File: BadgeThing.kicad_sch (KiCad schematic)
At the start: 62 parts, among them J2 Ext 5V, J3 External 3V3, J4 SWD Header, J5 USB_C_Receptacle_USB2.0, J6 Connector_Generic_Conn_01x02, J7 Conn_01x06, SW1 ESP RESET, SW2 Left, SW3 Down, SW4 Select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

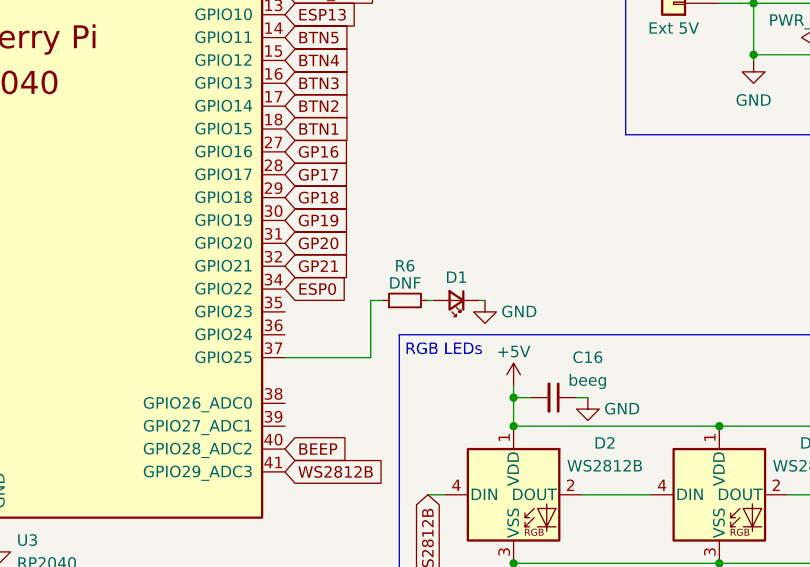
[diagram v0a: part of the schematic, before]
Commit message: Update 3D models
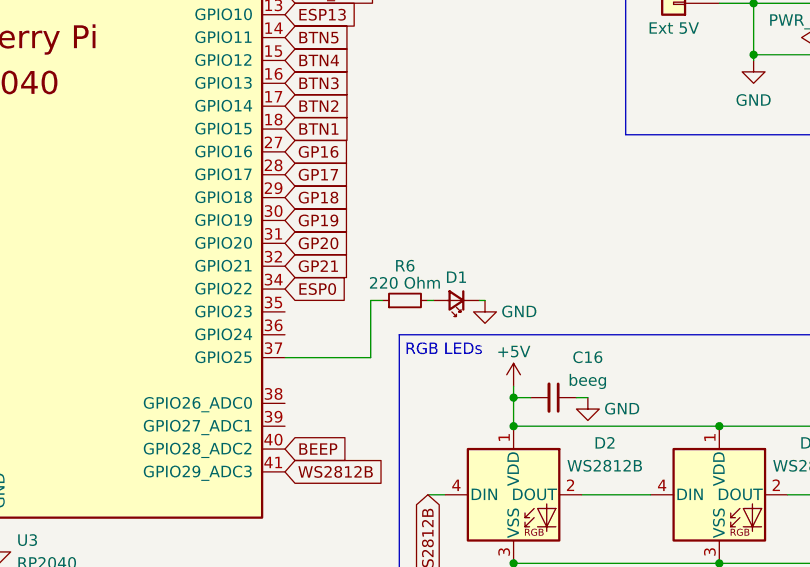
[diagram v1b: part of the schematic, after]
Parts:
- R6: value DNF -> 220 Ohm
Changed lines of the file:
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@@
       (effects (font (size 1.27 1.27)))
     )
-    (property "Value" "DNF" (at 167.005 113.665 90)
+    (property "Value" "220 Ohm" (at 167.005 113.665 90)
       (effects (font (size 1.27 1.27)))
     )

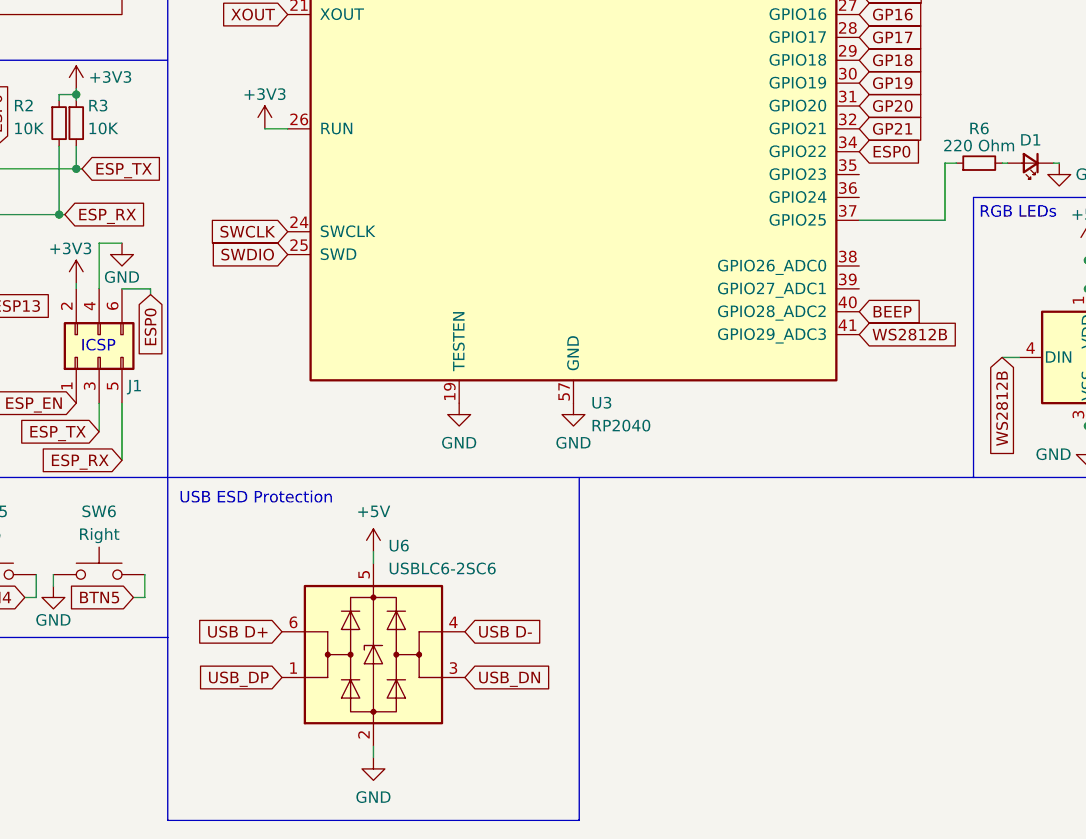
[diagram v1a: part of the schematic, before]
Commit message: consider adding an SD card slot
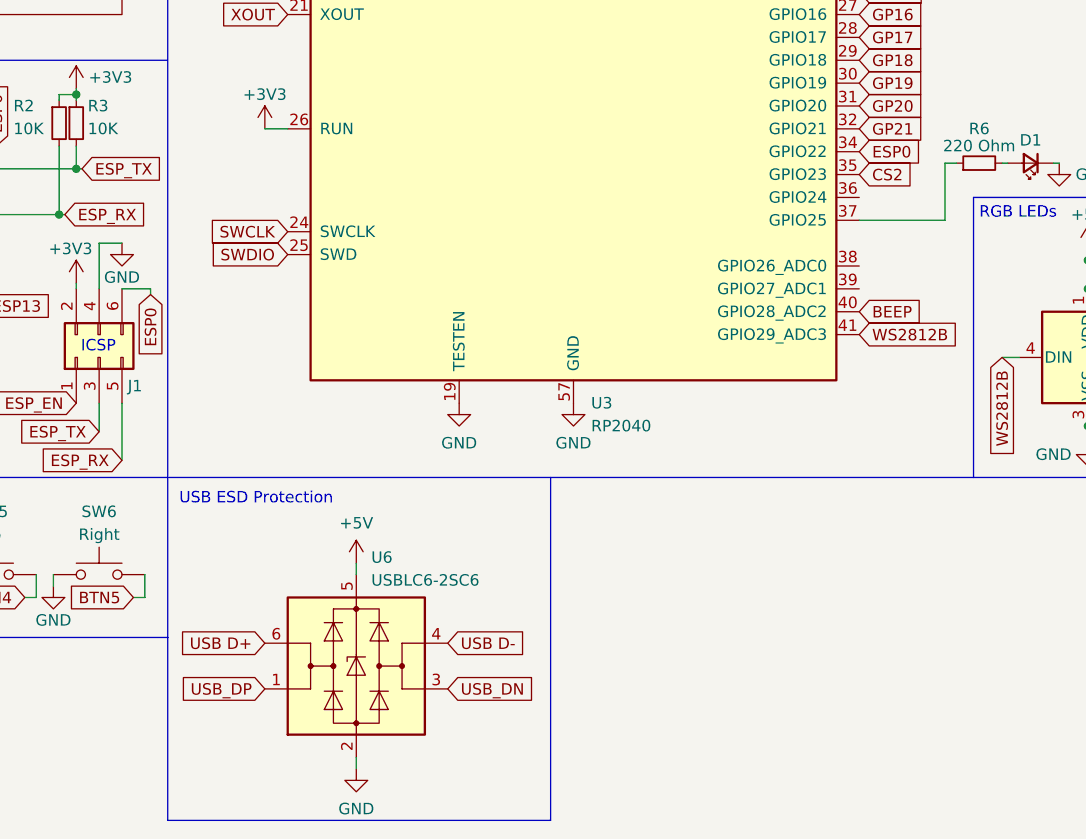
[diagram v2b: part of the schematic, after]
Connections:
- net CS2: now reaches U3.35 (GPIO23)
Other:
- moved on the sheet: U6
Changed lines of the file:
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@@
     (stroke (width 0) (type default))
   )
-  (polyline (pts (xy 76.835 188.595) (xy 122.555 188.595))
+  (polyline (pts (xy 76.835 188.595) (xy 119.38 188.595))
     (stroke (width 0) (type default))
   )
-  (wire (pts (xy 99.695 180.34) (xy 99.695 181.61))
+  (wire (pts (xy 97.79 181.61) (xy 97.79 182.88))
     (stroke (width 0) (type default))
   )
@@
     (stroke (width 0) (type default))
   )
-  (polyline (pts (xy 122.555 188.595) (xy 122.555 150.495))
+  (polyline (pts (xy 119.38 188.595) (xy 119.38 150.495))
     (stroke (width 0) (type default))
   )
@@
     (stroke (width 0) (type default))
   )
-  (wire (pts (xy 99.695 158.75) (xy 99.695 160.02))
+  (wire (pts (xy 97.79 160.02) (xy 97.79 161.29))
     (stroke (width 0) (type default))
   )
@@
     )
   )
-  (global_label "USB D-" (shape input) (at 109.855 167.64 0) (fields_autoplaced)
+  (global_label "USB D-" (shape input) (at 107.95 168.91 0) (fields_autoplaced)
     (effects (font (size 1.27 1.27)) (justify left))
-    (property "Intersheetrefs" "${INTERSHEET_REFS}" (at 120.3808 167.64 0)
+    (property "Intersheetrefs" "${INTERSHEET_REFS}" (at 118.4758 168.91 0)
       (effects (font (size 1.27 1.27)) (justify left) hide)
     )
@@
     )
   )
-  (global_label "USB_DP" (shape input) (at 89.535 172.72 180) (fields_autoplaced)
+  (global_label "USB_DP" (shape input) (at 87.63 173.99 180) (fields_autoplaced)
     (effects (font (size 1.27 1.27)) (justify right))
-    (property "Intersheetrefs" "${INTERSHEET_REFS}" (at 79.3116 172.72 0)
+    (property "Intersheetrefs" "${INTERSHEET_REFS}" (at 77.4066 173.99 0)
       (effects (font (size 1.27 1.27)) (justify right) hide)
     )
@@
     )
   )
+  (global_label "CS2" (shape input) (at 153.67 116.84 0) (fields_autoplaced)
+    (effects (font (size 1.27 1.27)) (justify left))
+    (property "Intersheetrefs" "${INTERSHEET_REFS}" (at 160.2648 116.84 0)
+      (effects (font (size 1.27 1.27)) (justify left) hide)
+    )
+  )
   (global_label "BEEP" (shape input) (at 273.685 125.095 180) (fields_autoplaced)
     (effects (font (size 1.27 1.27)) (justify right))
@@
     )
   )
-  (global_label "USB_DN" (shape input) (at 109.855 172.72 0) (fields_autoplaced)
+  (global_label "USB_DN" (shape input) (at 107.95 173.99 0) (fields_autoplaced)
     (effects (font (size 1.27 1.27)) (justify left))
-    (property "Intersheetrefs" "${INTERSHEET_REFS}" (at 120.1389 172.72 0)
+    (property "Intersheetrefs" "${INTERSHEET_REFS}" (at 118.2339 173.99 0)
       (effects (font (size 1.27 1.27)) (justify left) hide)
     )
@@
     )
   )
-  (global_label "USB D+" (shape input) (at 89.535 167.64 180) (fields_autoplaced)
+  (global_label "USB D+" (shape input) (at 87.63 168.91 180) (fields_autoplaced)
     (effects (font (size 1.27 1.27)) (justify right))
-    (property "Intersheetrefs" "${INTERSHEET_REFS}" (at 79.0092 167.64 0)
+    (property "Intersheetrefs" "${INTERSHEET_REFS}" (at 77.1042 168.91 0)
       (effects (font (size 1.27 1.27)) (justify right) hide)
     )
@@
     )
   )
-  (symbol (lib_name "+5V_2") (lib_id "power:+5V") (at 99.695 158.75 0) (unit 1)
+  (symbol (lib_name "+5V_2") (lib_id "power:+5V") (at 97.79 160.02 0) (unit 1)
     (in_bom yes) (on_board yes) (dnp no) (fields_autoplaced)
-    (property "Reference" "#PWR044" (at 99.695 162.56 0)
+    (property "Reference" "#PWR044" (at 97.79 163.83 0)
       (effects (font (size 1.27 1.27)) hide)
     )
-    (property "Value" "+5V" (at 99.695 154.305 0)
+    (property "Value" "+5V" (at 97.79 155.575 0)
       (effects (font (size 1.27 1.27)))
     )
-    (property "Footprint" "" (at 99.695 158.75 0)
+    (property "Footprint" "" (at 97.79 160.02 0)
       (effects (font (size 1.27 1.27)) hide)
     )
-    (property "Datasheet" "" (at 99.695 158.75 0)
+    (property "Datasheet" "" (at 97.79 160.02 0)
       (effects (font (size 1.27 1.27)) hide)
     )
@@
     )
   )
-  (symbol (lib_id "Power_Protection:USBLC6-2SC6") (at 99.695 170.18 0) (unit 1)
+  (symbol (lib_id "Power_Protection:USBLC6-2SC6") (at 97.79 171.45 0) (unit 1)
     (in_bom yes) (on_board yes) (dnp no) (fields_autoplaced)
-    (property "Reference" "U6" (at 101.3461 158.115 0)
+    (property "Reference" "U6" (at 99.4411 159.385 0)
       (effects (font (size 1.27 1.27)) (justify left))
     )
-    (property "Value" "USBLC6-2SC6" (at 101.3461 160.655 0)
+    (property "Value" "USBLC6-2SC6" (at 99.4411 161.925 0)
       (effects (font (size 1.27 1.27)) (justify left))
     )
-    (property "Footprint" "Package_TO_SOT_SMD:SOT-23-6" (at 99.695 182.88 0)
+    (property "Footprint" "Package_TO_SOT_SMD:SOT-23-6" (at 97.79 184.15 0)
       (effects (font (size 1.27 1.27)) hide)
     )
-    (property "Datasheet" "https://www.st.com/resource/en/datasheet/usblc6-2.pdf" (at 104.775 161.29 0)
+    (property "Datasheet" "https://www.st.com/resource/en/datasheet/usblc6-2.pdf" (at 102.87 162.56 0)
       (effects (font (size 1.27 1.27)) hide)
     )
-    (property "LCSC" "C2687116" (at 99.695 170.18 0)
+    (property "LCSC" "C2687116" (at 97.79 171.45 0)
       (effects (font (size 1.27 1.27)) hide)
     )
@@
     )
   )
-  (symbol (lib_id "power:GND") (at 99.695 181.61 0) (unit 1)
+  (symbol (lib_id "power:GND") (at 97.79 182.88 0) (unit 1)
     (in_bom yes) (on_board yes) (dnp no) (fields_autoplaced)
-    (property "Reference" "#PWR045" (at 99.695 187.96 0)
+    (property "Reference" "#PWR045" (at 97.79 189.23 0)
       (effects (font (size 1.27 1.27)) hide)
     )
-    (property "Value" "GND" (at 99.695 186.055 0)
+    (property "Value" "GND" (at 97.79 187.325 0)
       (effects (font (size 1.27 1.27)))
     )
-    (property "Footprint" "" (at 99.695 181.61 0)
+    (property "Footprint" "" (at 97.79 182.88 0)
       (effects (font (size 1.27 1.27)) hide)
     )
-    (property "Datasheet" "" (at 99.695 181.61 0)
+    (property "Datasheet" "" (at 97.79 182.88 0)
       (effects (font (size 1.27 1.27)) hide)
     )

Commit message: Actual final real finishing touches (+test pads)
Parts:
- added J10, J11, J12, J8, J9: Conn_01x01, Connector_PinHeader_2.00mm:PinHeader_1x01_P2.00mm_Vertical, symbol Connector_Generic:Conn_01x01
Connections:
- net +3V3: now also J12.1 (Pin_1)
- net +5V: now also J11.1 (Pin_1)
- net MISO: now also J8.1 (Pin_1)
- net MOSI: now also J9.1 (Pin_1)
- net SCLK: now also J10.1 (Pin_1)
- net CS2: no longer names the net of U3.35 (GPIO23)
- no-connect marks 24 -> 29
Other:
- note added: "Test Points"
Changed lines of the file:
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@@
   (no_connect (at 269.875 100.33))
   (no_connect (at 55.88 139.065))
+  (no_connect (at 153.67 127))
   (no_connect (at 45.085 83.82))
   (no_connect (at 55.88 133.985))
@@
   (no_connect (at 55.88 128.905))
   (no_connect (at 45.085 76.2))
+  (no_connect (at 153.67 66.04))
+  (no_connect (at 153.67 129.54))
+  (no_connect (at 153.67 119.38))
+  (no_connect (at 153.67 116.84))
   (wire (pts (xy 45.085 45.72) (xy 43.815 45.72))
     (stroke (width 0) (type default))
@@
     (stroke (width 0) (type default))
   )
+  (wire (pts (xy 132.08 170.18) (xy 128.905 170.18))
+    (stroke (width 0) (type default))
+  )
   (wire (pts (xy 194.31 43.18) (xy 198.12 43.18))
     (stroke (width 0) (type default))
@@
     (stroke (width 0) (type default))
   )
+  (wire (pts (xy 122.555 166.37) (xy 132.08 166.37))
+    (stroke (width 0) (type default))
+  )
   (wire (pts (xy 155.575 38.1) (xy 155.575 31.75))
     (stroke (width 0) (type default))
@@
     (stroke (width 0) (type default))
   )
+  (wire (pts (xy 132.08 168.91) (xy 132.08 170.18))
+    (stroke (width 0) (type default))
+  )
   (wire (pts (xy 43.815 60.96) (xy 43.815 63.5))
     (stroke (width 0) (type default))
@@
     (effects (font (size 1.27 1.27)) (justify left bottom))
   )
+  (text "Test Points" (at 120.65 153.67 0)
+    (effects (font (size 1.27 1.27)) (justify left bottom))
+  )
   (text "Voltage Regulator" (at 193.802 64.2874 0)
     (effects (font (size 1.27 1.27)) (justify left bottom))
@@
     )
   )
+  (global_label "SCLK" (shape input) (at 132.08 163.83 180) (fields_autoplaced)
+    (effects (font (size 1.27 1.27)) (justify right))
+    (property "Intersheetrefs" "${INTERSHEET_REFS}" (at 124.3966 163.83 0)
+      (effects (font (size 1.27 1.27)) (justify right) hide)
+    )
+  )
   (global_label "SCLK" (shape input) (at 26.035 66.04 180) (fields_autoplaced)
     (effects (font (size 1.27 1.27)) (justify right))
@@
     )
   )
+  (global_label "MOSI" (shape input) (at 132.08 161.29 180) (fields_autoplaced)
+    (effects (font (size 1.27 1.27)) (justify right))
+    (property "Intersheetrefs" "${INTERSHEET_REFS}" (at 124.578 161.29 0)
+      (effects (font (size 1.27 1.27)) (justify right) hide)
+    )
+  )
   (global_label "ESP_TX" (shape input) (at 69.215 145.415 180) (fields_autoplaced)
     (effects (font (size 1.27 1.27)) (justify right))
@@
     )
   )
-  (global_label "CS2" (shape input) (at 153.67 116.84 0) (fields_autoplaced)
-    (effects (font (size 1.27 1.27)) (justify left))
-    (property "Intersheetrefs" "${INTERSHEET_REFS}" (at 160.2648 116.84 0)
-      (effects (font (size 1.27 1.27)) (justify left) hide)
-    )
-  )
   (global_label "BEEP" (shape input) (at 273.685 125.095 180) (fields_autoplaced)
     (effects (font (size 1.27 1.27)) (justify right))
@@
     )
   )
+  (global_label "MISO" (shape input) (at 132.08 158.75 180) (fields_autoplaced)
+    (effects (font (size 1.27 1.27)) (justify right))
+    (property "Intersheetrefs" "${INTERSHEET_REFS}" (at 124.578 158.75 0)
+      (effects (font (size 1.27 1.27)) (justify right) hide)
+    )
+  )
   (global_label "GP20" (shape input) (at 153.67 109.22 0) (fields_autoplaced)
     (effects (font (size 1.27 1.27)) (justify left))
@@
     )
   )
+  (symbol (lib_id "Connector_Generic:Conn_01x01") (at 137.16 158.75 0) (unit 1)
+    (in_bom yes) (on_board yes) (dnp no)
+    (property "Reference" "J8" (at 139.065 153.67 0)
+      (effects (font (size 1.27 1.27)) (justify left))
+    )
+    (property "Value" "Conn_01x01" (at 139.065 155.575 0)
+      (effects (font (size 1.27 1.27)) (justify left))
+    )
+    (property "Footprint" "Connector_PinHeader_2.00mm:PinHeader_1x01_P2.00mm_Vertical" (at 137.16 158.75 0)
+      (effects (font (size 1.27 1.27)) hide)
+    )
+    (property "Datasheet" "~" (at 137.16 158.75 0)
+      (effects (font (size 1.27 1.27)) hide)
+    )
+    (pin "1")
+    (instances
+      (project "BadgeThing"
+        (path "/35d5f6bf-e39e-48ab-813a-17587fce37db"
+          (reference "J8") (unit 1)
+        )
+      )
+    )
+  )
   (symbol (lib_id "power:GND") (at 40.64 146.685 0) (unit 1)
     (in_bom yes) (on_board yes) (dnp no)
@@
     )
   )
+  (symbol (lib_id "power:+3V3") (at 128.905 170.18 0) (unit 1)
+    (in_bom yes) (on_board yes) (dnp no)
+    (property "Reference" "#PWR047" (at 128.905 173.99 0)
+      (effects (font (size 1.27 1.27)) hide)
+    )
+    (property "Value" "+3V3" (at 125.095 168.91 0)
+      (effects (font (size 1.27 1.27)))
+    )
+    (property "Footprint" "" (at 128.905 170.18 0)
+      (effects (font (size 1.27 1.27)) hide)
+    )
+    (property "Datasheet" "" (at 128.905 170.18 0)
+      (effects (font (size 1.27 1.27)) hide)
+    )
+    (pin "1")
+    (instances
+      (project "BadgeThing"
+        (path "/35d5f6bf-e39e-48ab-813a-17587fce37db"
+          (reference "#PWR047") (unit 1)
+        )
+      )
+    )
+  )
+  (symbol (lib_id "Connector_Generic:Conn_01x01") (at 137.16 166.37 0) (unit 1)
+    (in_bom yes) (on_board yes) (dnp no)
+    (property "Reference" "J11" (at 139.065 167.005 0)
+      (effects (font (size 1.27 1.27)) (justify left))
+    )
+    (property "Value" "Conn_01x01" (at 139.065 168.91 0)
+      (effects (font (size 1.27 1.27)) (justify left))
+    )
+    (property "Footprint" "Connector_PinHeader_2.00mm:PinHeader_1x01_P2.00mm_Vertical" (at 137.16 166.37 0)
+      (effects (font (size 1.27 1.27)) hide)
+    )
+    (property "Datasheet" "~" (at 137.16 166.37 0)
+      (effects (font (size 1.27 1.27)) hide)
+    )
+    (pin "1")
+    (instances
+      (project "BadgeThing"
+        (path "/35d5f6bf-e39e-48ab-813a-17587fce37db"
+          (reference "J11") (unit 1)
+        )
+      )
+    )
+  )
   (symbol (lib_id "Device:C_Small") (at 193.04 21.59 0) (unit 1)
     (in_bom yes) (on_board yes) (dnp no)
@@
     )
   )
+  (symbol (lib_id "Connector_Generic:Conn_01x01") (at 137.16 161.29 0) (unit 1)
+    (in_bom yes) (on_board yes) (dnp no)
+    (property "Reference" "J9" (at 139.065 158.115 0)
+      (effects (font (size 1.27 1.27)) (justify left))
+    )
+    (property "Value" "Conn_01x01" (at 139.065 160.02 0)
+      (effects (font (size 1.27 1.27)) (justify left))
+    )
+    (property "Footprint" "Connector_PinHeader_2.00mm:PinHeader_1x01_P2.00mm_Vertical" (at 137.16 161.29 0)
+      (effects (font (size 1.27 1.27)) hide)
+    )
+    (property "Datasheet" "~" (at 137.16 161.29 0)
+      (effects (font (size 1.27 1.27)) hide)
+    )
+    (pin "1")
+    (instances
+      (project "BadgeThing"
+        (path "/35d5f6bf-e39e-48ab-813a-17587fce37db"
+          (reference "J9") (unit 1)
+        )
+      )
+    )
+  )
   (symbol (lib_id "Switch:SW_Push") (at 69.215 161.29 0) (unit 1)
     (in_bom yes) (on_board yes) (dnp no)
@@
     )
   )
+  (symbol (lib_id "Connector_Generic:Conn_01x01") (at 137.16 163.83 0) (unit 1)
+    (in_bom yes) (on_board yes) (dnp no)
+    (property "Reference" "J10" (at 139.065 162.56 0)
+      (effects (font (size 1.27 1.27)) (justify left))
+    )
+    (property "Value" "Conn_01x01" (at 139.065 164.465 0)
+      (effects (font (size 1.27 1.27)) (justify left))
+    )
+    (property "Footprint" "Connector_PinHeader_2.00mm:PinHeader_1x01_P2.00mm_Vertical" (at 137.16 163.83 0)
+      (effects (font (size 1.27 1.27)) hide)
+    )
+    (property "Datasheet" "~" (at 137.16 163.83 0)
+      (effects (font (size 1.27 1.27)) hide)
+    )
+    (pin "1")
+    (instances
+      (project "BadgeThing"
+        (path "/35d5f6bf-e39e-48ab-813a-17587fce37db"
+          (reference "J10") (unit 1)
+        )
+      )
+    )
+  )
   (symbol (lib_id "power:GND") (at 41.91 19.05 0) (unit 1)
     (in_bom yes) (on_board yes) (dnp no)
@@
     )
   )
+  (symbol (lib_id "Connector_Generic:Conn_01x01") (at 137.16 168.91 0) (unit 1)
+    (in_bom yes) (on_board yes) (dnp no)
+    (property "Reference" "J12" (at 139.065 171.45 0)
+      (effects (font (size 1.27 1.27)) (justify left))
+    )
+    (property "Value" "Conn_01x01" (at 139.065 173.355 0)
+      (effects (font (size 1.27 1.27)) (justify left))
+    )
+    (property "Footprint" "Connector_PinHeader_2.00mm:PinHeader_1x01_P2.00mm_Vertical" (at 137.16 168.91 0)
+      (effects (font (size 1.27 1.27)) hide)
+    )
+    (property "Datasheet" "~" (at 137.16 168.91 0)
+      (effects (font (size 1.27 1.27)) hide)
+    )
+    (pin "1")
+    (instances
+      (project "BadgeThing"
+        (path "/35d5f6bf-e39e-48ab-813a-17587fce37db"
+          (reference "J12") (unit 1)
+        )
+      )
+    )
+  )
   (symbol (lib_id "Switch:SW_Push") (at 33.02 161.29 0) (unit 1)
     (in_bom yes) (on_board yes) (dnp no)
@@
         )
       )
+    )
+  )
+  (symbol (lib_name "+5V_3") (lib_id "power:+5V") (at 122.555 166.37 0) (unit 1)
+    (in_bom yes) (on_board yes) (dnp no) (fields_autoplaced)
+    (property "Reference" "#PWR046" (at 122.555 170.18 0)
+      (effects (font (size 1.27 1.27)) hide)
+    )
+    (property "Value" "+5V" (at 122.555 162.56 0)
+      (effects (font (size 1.27 1.27)))
+    )
+    (property "Footprint" "" (at 122.555 166.37 0)
+      (effects (font (size 1.27 1.27)) hide)
+    )
+    (property "Datasheet" "" (at 122.555 166.37 0)
+      (effects (font (size 1.27 1.27)) hide)
+    )
+    (pin "1")
+    (instances
+      (project "BadgeThing"
+        (path "/35d5f6bf-e39e-48ab-813a-17587fce37db"
+          (reference "#PWR046") (unit 1)
+        )
+      )
